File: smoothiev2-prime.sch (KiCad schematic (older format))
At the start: 142 parts, among them J1 USB_B, J10 Conn_01x02, J15 Conn_01x02, J2 USB_A, J3 Micro_SD_Card_Det, J30 Conn_01x03_Male, J41 Conn_ARM_JTAG_SWD_10, J42 Conn_01x02, J43 Conn_01x02, J5 Screw_Terminal_01x04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

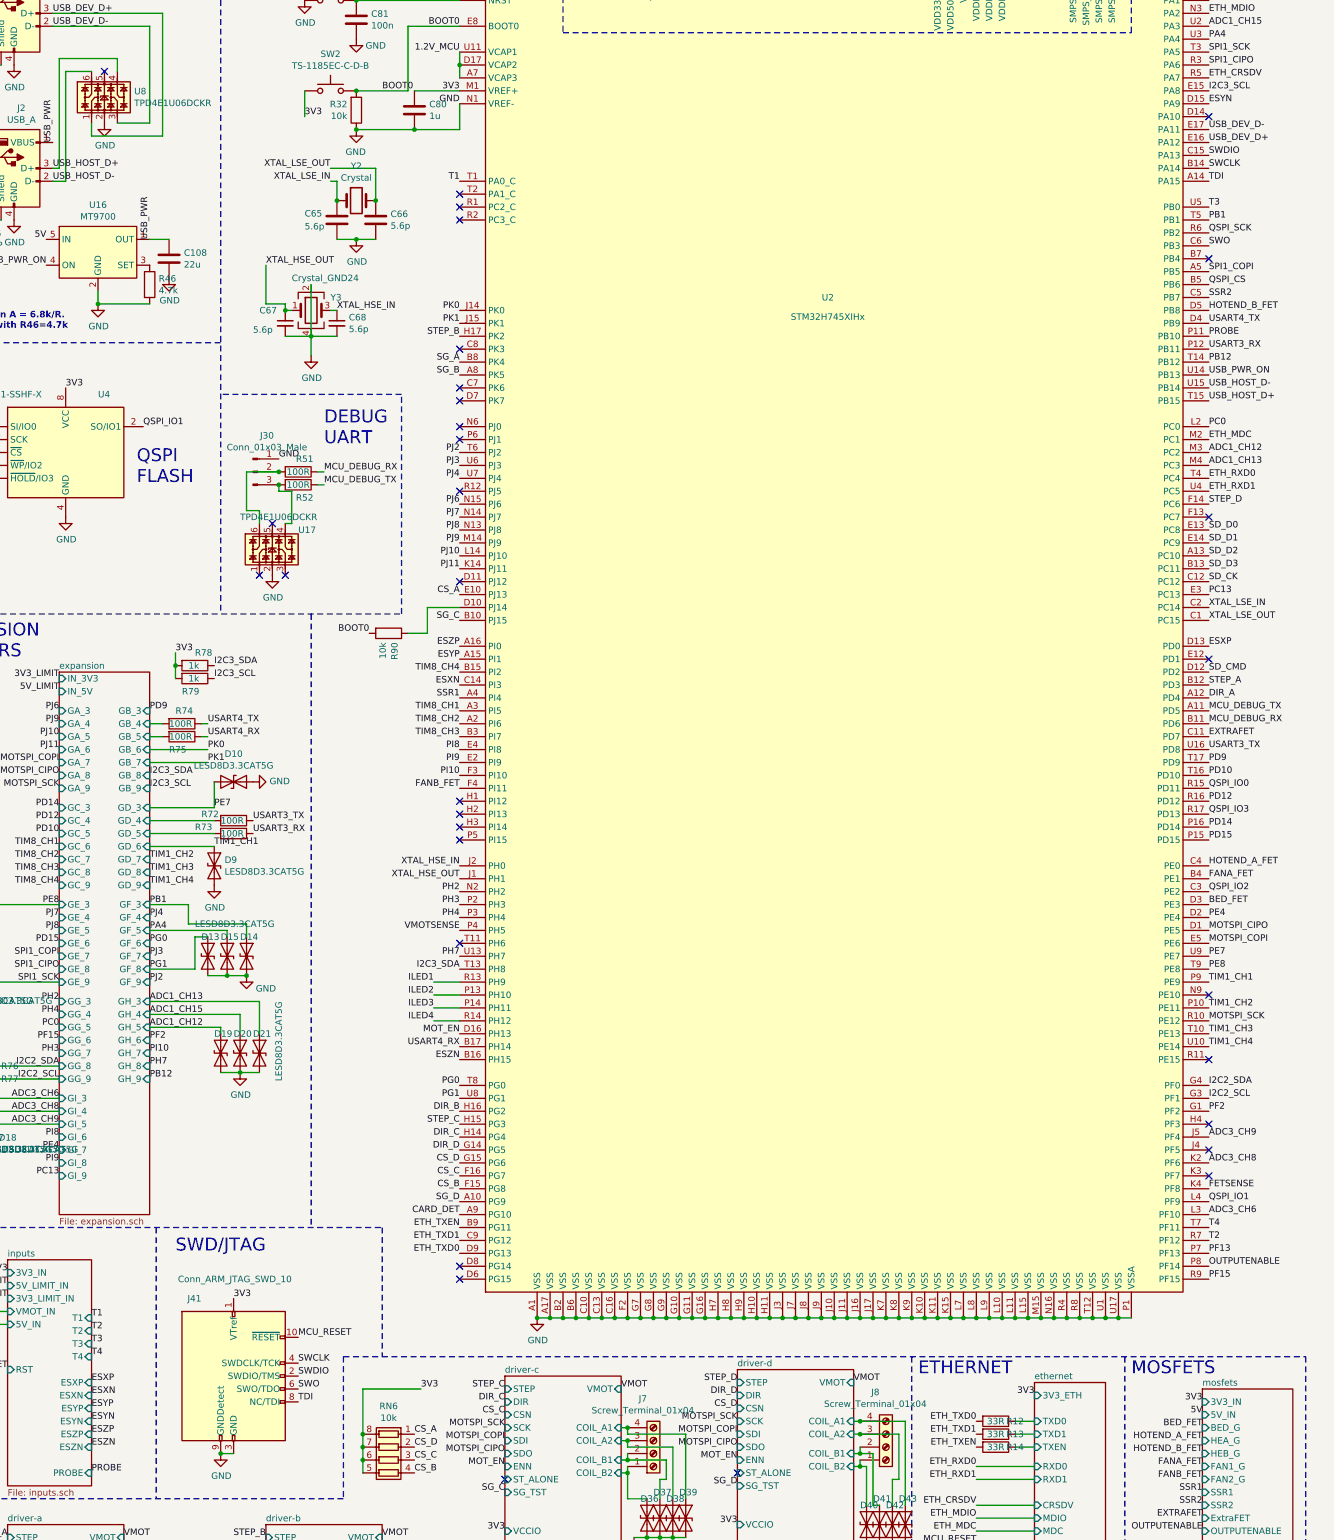
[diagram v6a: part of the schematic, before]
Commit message: Revision3 - Fix 5V cascading problem, change ADC opamp supply to 5V, add comparator to probe input, pulldown FETs when their MCU pins float.
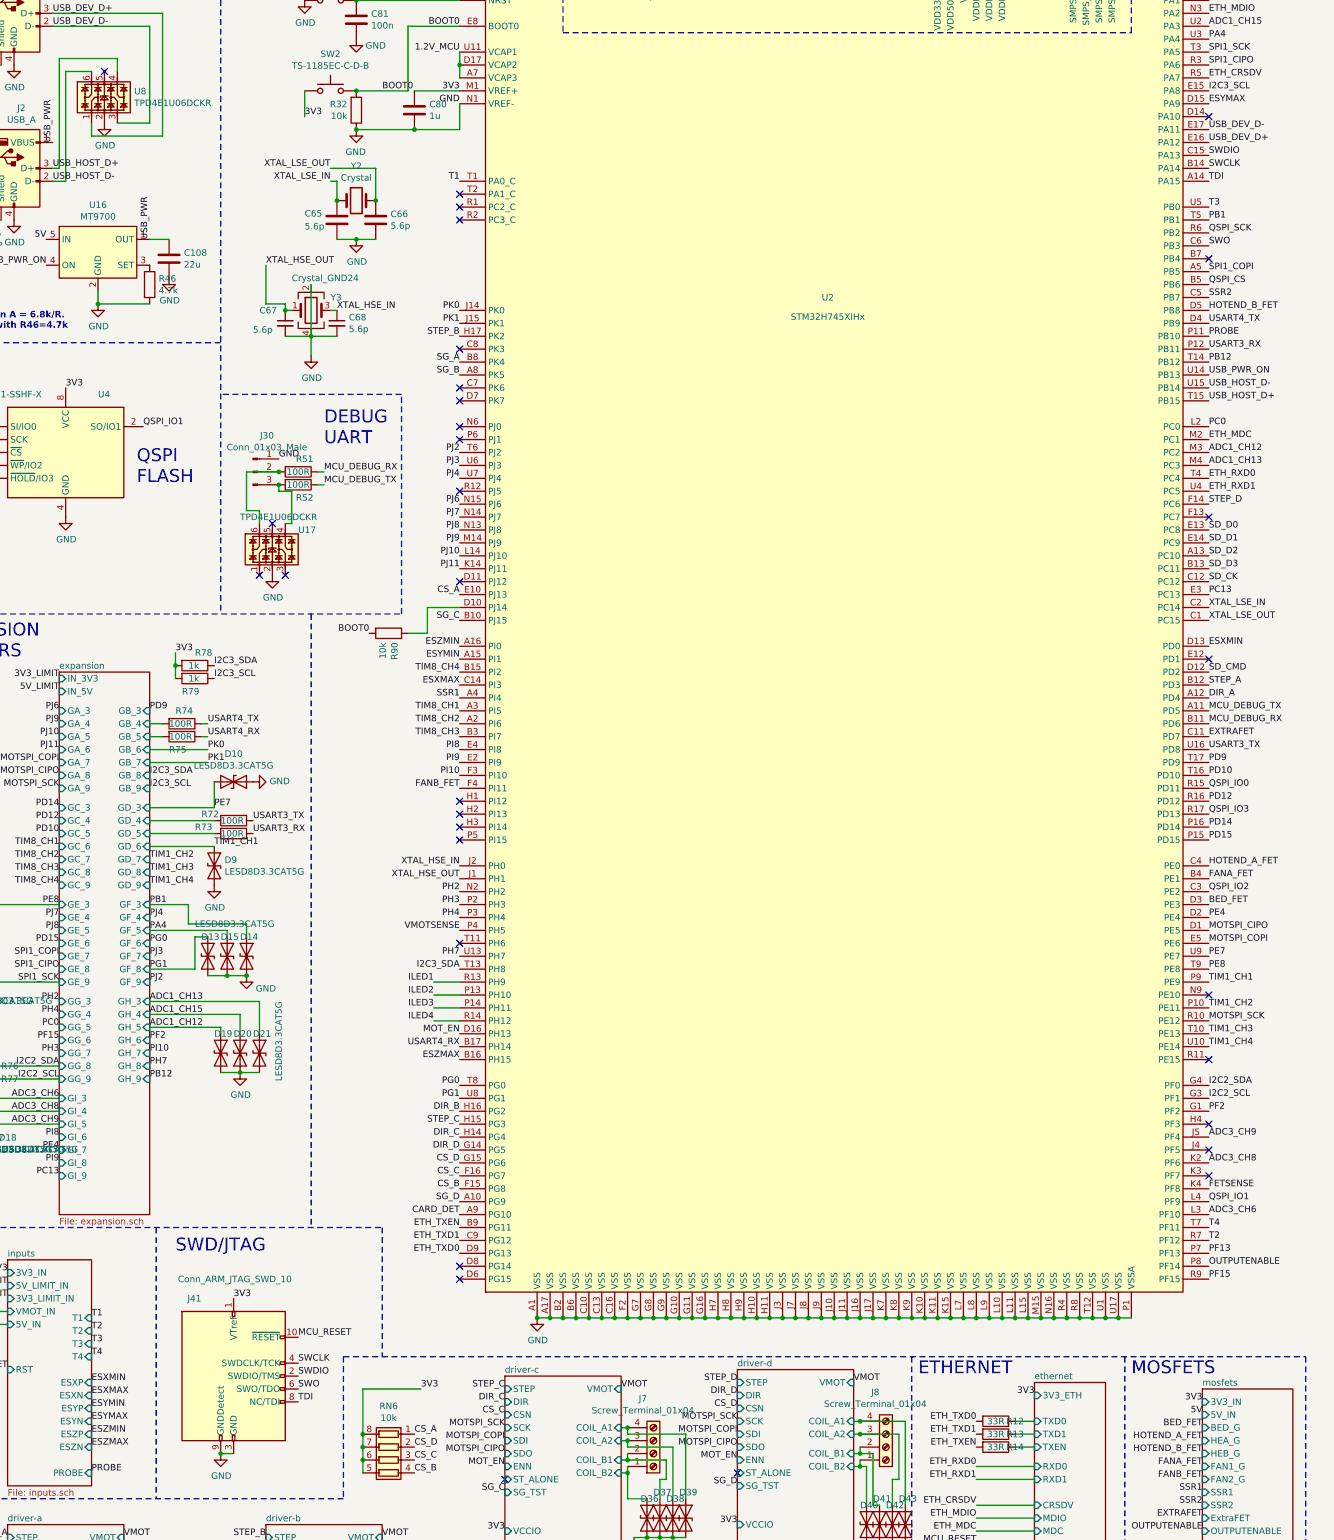
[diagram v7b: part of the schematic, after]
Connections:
- net at U2.E1 (SMPS_VLX): now also C69.1, L2.2
- net ESXN renamed ESXMAX
- net ESXP renamed ESXMIN
- net ESYN renamed ESYMAX
- net ESYP renamed ESYMIN
- net ESZN renamed ESZMAX
- net ESZP renamed ESZMIN
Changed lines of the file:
@@
 $EndSheet
 Text Label 1800 13250 0    50   ~ 0
-ESXP
+ESXMIN
 Text Label 1800 13350 0    50   ~ 0
-ESXN
+ESXMAX
 Text Label 4650 7850 2    50   ~ 0
-ESXN
+ESXMAX
 Text Label 10450 5450 0    50   ~ 0
 USB_PWR_ON
 Text Label 1800 13450 0    50   ~ 0
-ESYP
+ESYMIN
 Text Label 1800 13550 0    50   ~ 0
-ESYN
+ESYMAX
 Text Label 1800 13750 0    50   ~ 0
-ESZN
+ESZMAX
 Text Label 1800 13650 0    50   ~ 0
-ESZP
+ESZMIN
 Text Label 4650 7650 2    50   ~ 0
-ESYP
+ESYMIN
 Text Label 10450 3350 0    50   ~ 0
-ESYN
+ESYMAX
 Text Label 4650 7550 2    50   ~ 0
-ESZP
+ESZMIN
 Text Label 10450 7850 0    50   ~ 0
 STEP_A
@@
 QSPI_IO0
 Text Label 4650 10750 2    50   ~ 0
-ESZN
+ESZMAX
 Text Label 10450 7550 0    50   ~ 0
-ESXP
+ESXMIN
 Text Label 4650 7350 2    50   ~ 0
 SG_C

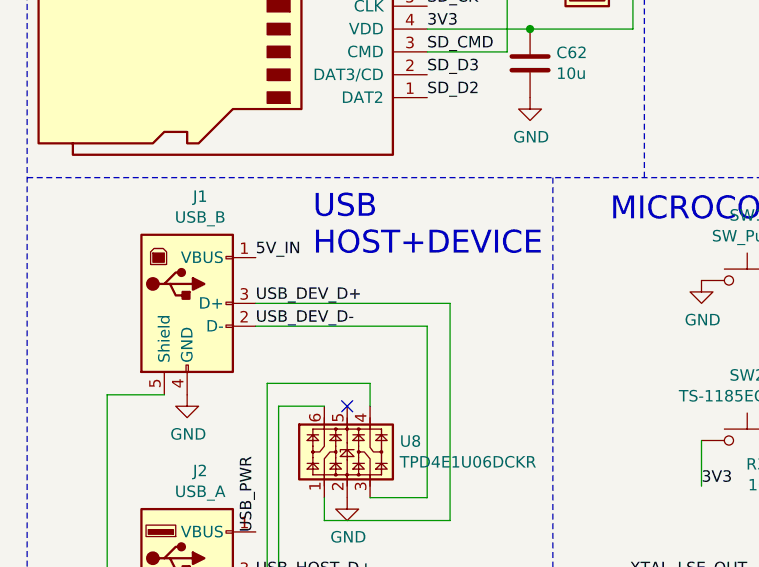
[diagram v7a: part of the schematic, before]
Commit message: Add power monitor circuit to VMOT DC/DC, add disconnect jumper to 5V_IN USB.
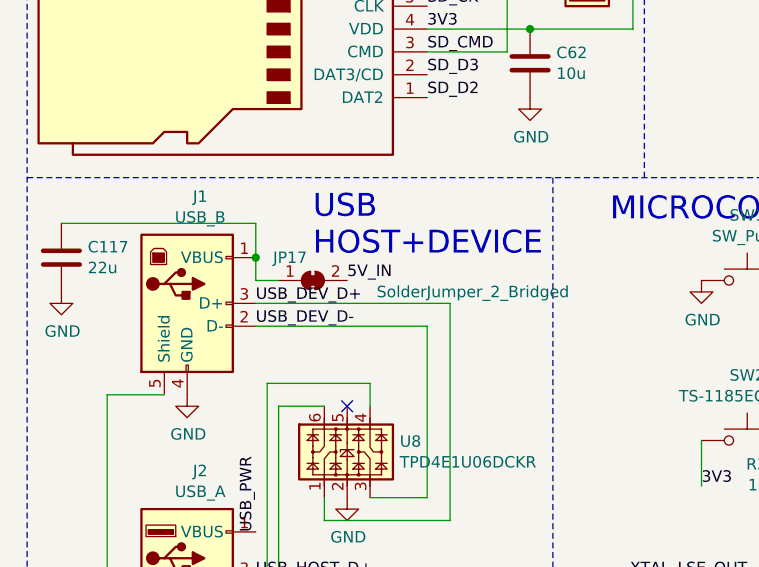
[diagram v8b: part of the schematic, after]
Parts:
- added C117: 22u, Capacitor_SMD:C_0805_2012Metric, symbol Device:C
- added JP17: SolderJumper_2_Bridged, Jumper:SolderJumper-2_P1.3mm_Bridged2Bar_Pad1.0x1.5mm, symbol Jumper:SolderJumper_2_Bridged
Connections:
- net 5V_IN: now also JP17.2 (B); no longer J1.1 (VBUS)
- net GND: now also C117.2
- net at U2.E1 (SMPS_VLX): now also C69.1, L2.2
- new net: C117.1, J1.1 (VBUS), JP17.1 (A)
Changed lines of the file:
@@
 Text Label 10450 9050 0    50   ~ 0
 PD15
-Text Label 1500 2450 0    50   ~ 0
-5V_IN
 Text Label 4650 2750 2    50   ~ 0
 BOOT0
@@
 Wire Wire Line
 	1050 12800 1150 12800
+$Comp
+L Jumper:SolderJumper_2_Bridged JP17
+U 1 1 62582F65
+P 1750 2550
+F 0 "JP17" H 1650 2650 50  0000 C CNN
+F 1 "SolderJumper_2_Bridged" H 2450 2500 50  0000 C CNN
+F 2 "Jumper:SolderJumper-2_P1.3mm_Bridged2Bar_Pad1.0x1.5mm" H 1750 2550 50  0001 C CNN
+F 3 "~" H 1750 2550 50  0001 C CNN
+	1    1750 2550
+	1    0    0    -1
+$EndComp
+Wire Wire Line
+	1600 2550 1500 2550
+Wire Wire Line
+	1500 2550 1500 2450
+Text Label 1900 2550 0    50   ~ 0
+5V_IN
+$Comp
+L Device:C C?
+U 1 1 625ECF17
+P 650 2450
+AR Path="/631D7D17/625ECF17" Ref="C?"  Part="1"
+AR Path="/625ECF17" Ref="C117"  Part="1"
+F 0 "C117" H 765 2496 50  0000 L CNN
+F 1 "22u" H 765 2405 50  0000 L CNN
+F 2 "Capacitor_SMD:C_0805_2012Metric" H 688 2300 50  0001 C CNN
+F 3 "~" H 650 2450 50  0001 C CNN
+	1    650  2450
+	1    0    0    -1
+$EndComp
+Wire Wire Line
+	650  2300 1500 2300
+Wire Wire Line
+	1500 2300 1500 2450
+Connection ~ 1500 2450
+$Comp
+L power:GND #PWR075
+U 1 1 62665763
+P 650 2600
+F 0 "#PWR075" H 650 2350 50  0001 C CNN
+F 1 "GND" H 655 2427 50  0000 C CNN
+F 2 "" H 650 2600 50  0001 C CNN
+F 3 "" H 650 2600 50  0001 C CNN
+	1    650  2600
+	1    0    0    -1
+$EndComp
 $EndSCHEMATC
